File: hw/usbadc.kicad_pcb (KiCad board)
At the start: 4 copper layers, 100 x 60 mm, 346 parts, among them J1 USB_C_Receptacle_USB2.0, J2 BNC, J3 BNC, J4 T8_JTAG, J5 BNC, J7 BNC, J9 Expansion, K1 Tx2SA-5V, K2 Tx2SA-5V, Q1 SSM6N35AFE, Q2 SSM3K37MFV, Q3 SSM6N35AFE, Q4 SSM6P35AFE, Q5 SSM6P35AFE, SW1 Reconfig, U1 RT8096B, U10 AQY280S, U11 TS5A63157DBV, U12 OPA859xDSG, U13 AD8370, U14 AQY280S, U15 T20Q144xx, U16 USB3343, U17 NDS36PT5-16ET, U18 TS5A63157DBV, U19 OPA859xDSG, U2 RT8096B, U20 AD8370, U22 TSV992A, U23 MCP47CVB02-E_UN, U24 AT25FF081A-SSHN-B, U25 TLV75801PDBV, U26 TLV803EA29DBZR, U3 RT8096B, U4 SN74LVC2T45DCUR, U5 TPS563249DDC, U6 PCA9306DC1, U7 5P49V6965, U8 24AA0x, U9 MAX19517, X1 ECS-2520MV-260-CN-TR, Y1 25MHz

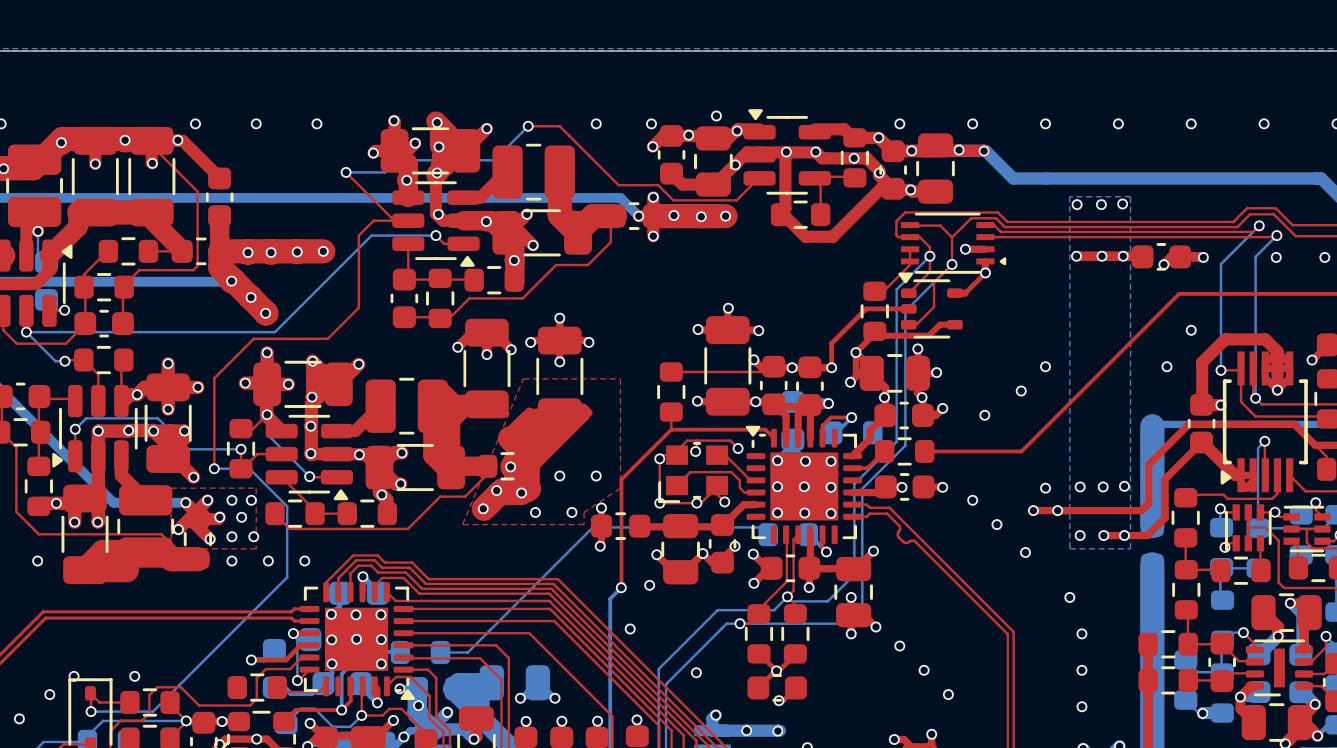
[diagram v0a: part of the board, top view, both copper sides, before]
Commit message: [hw] increased bypass caps on analog +/- supplies
Caps behind ferrite beads increased from 100n to 1u.
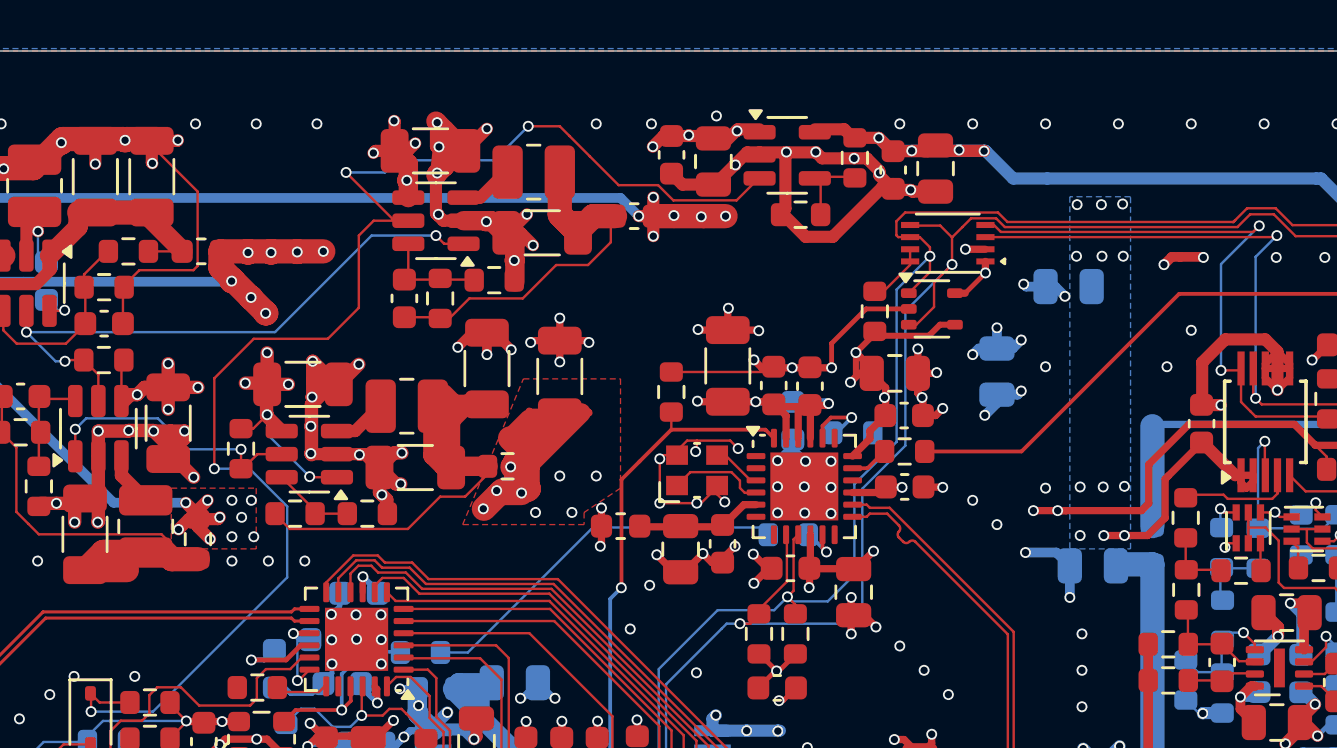
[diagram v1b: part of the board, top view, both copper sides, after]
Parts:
- added C146: 1u, Capacitor_SMD:C_0805_2012Metric, B.Cu at (115.0, 36.2)
- C101, C145: value 100n -> 1u; footprint Capacitor_SMD:C_0603_1608Metric -> Capacitor_SMD:C_0805_2012Metric; moved to B.Cu
- moved C145 39.0 mm to (119.0, 44.2), turned to 180 degrees
- moved C101 4.01 mm to (118.0, 32.7), turned to 180 degrees
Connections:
- C145 pad 1: -2V5_analog -> Vpp_analog
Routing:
- net GND: track 459.7 -> 463.8 mm, vias 415 -> 417
- net +2V5_analog: track 164.4 -> 161.7 mm
- net -2V5_analog: track 106.1 -> 107.6 mm, vias 35 -> 38
- net Vpp_analog: track 60.9 -> 62.3 mm

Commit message: [hw]: changed input AC-coupling cap from 100n->10n
Does not affect PCB
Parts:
- C66, C78: value 100n -> 10n
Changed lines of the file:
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@@
         (effects (font (size 1 1) (thickness 0.15)))
     )
-    (fp_text value "100n" (at 0 1.68) (layer "F.Fab")
+    (fp_text value "10n" (at 0 1.68) (layer "F.Fab")
         (effects (font (size 1 1) (thickness 0.15)))
     )
@@
         (effects (font (size 1 1) (thickness 0.15)))
     )
-    (fp_text value "100n" (at 0 1.68) (layer "F.Fab")
+    (fp_text value "10n" (at 0 1.68) (layer "F.Fab")
         (effects (font (size 1 1) (thickness 0.15)))
     )
